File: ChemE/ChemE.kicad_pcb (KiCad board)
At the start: 2 copper layers, 36 x 26 mm, 11 parts, among them IC1 LF353P, J1 Circuit Battery, Q1 MTP3055E, U1 LM393N

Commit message: made prod
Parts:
- renumbered motor1 to motor, batt_car1 to motor_batt
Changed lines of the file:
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@@
 		(descr "Through hole straight pin header, 1x02, 2.54mm pitch, single row")
 		(tags "Through hole pin header THT 1x02 2.54mm single row")
-		(property "Reference" "motor1"
+		(property "Reference" "motor"
 			(at -2.4384 1.1176 90)
 			(layer "F.SilkS")
@@
 		(descr "Through hole straight pin header, 1x02, 2.54mm pitch, single row")
 		(tags "Through hole pin header THT 1x02 2.54mm single row")
-		(property "Reference" "batt_car1"
-			(at 2.54 1.4224 180)
-			(layer "F.SilkS")
-			(effects
+		(property "Reference" "motor_batt"
+			(at 2.54 0.7576 180)
+			(layer "F.SilkS")
+			(effects

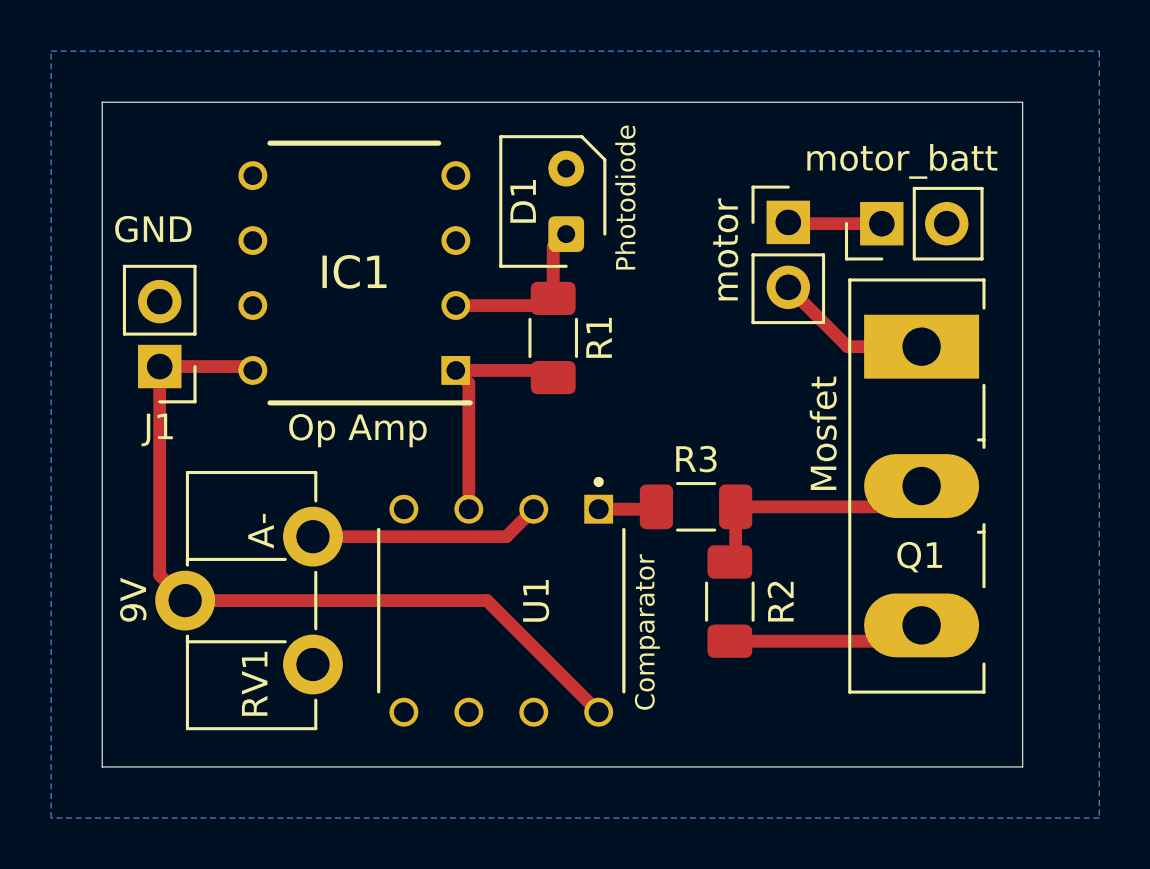
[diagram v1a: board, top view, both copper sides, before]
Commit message: increased trace width, made tht
increased trace width from .5mm to 1mm and made everything THT.
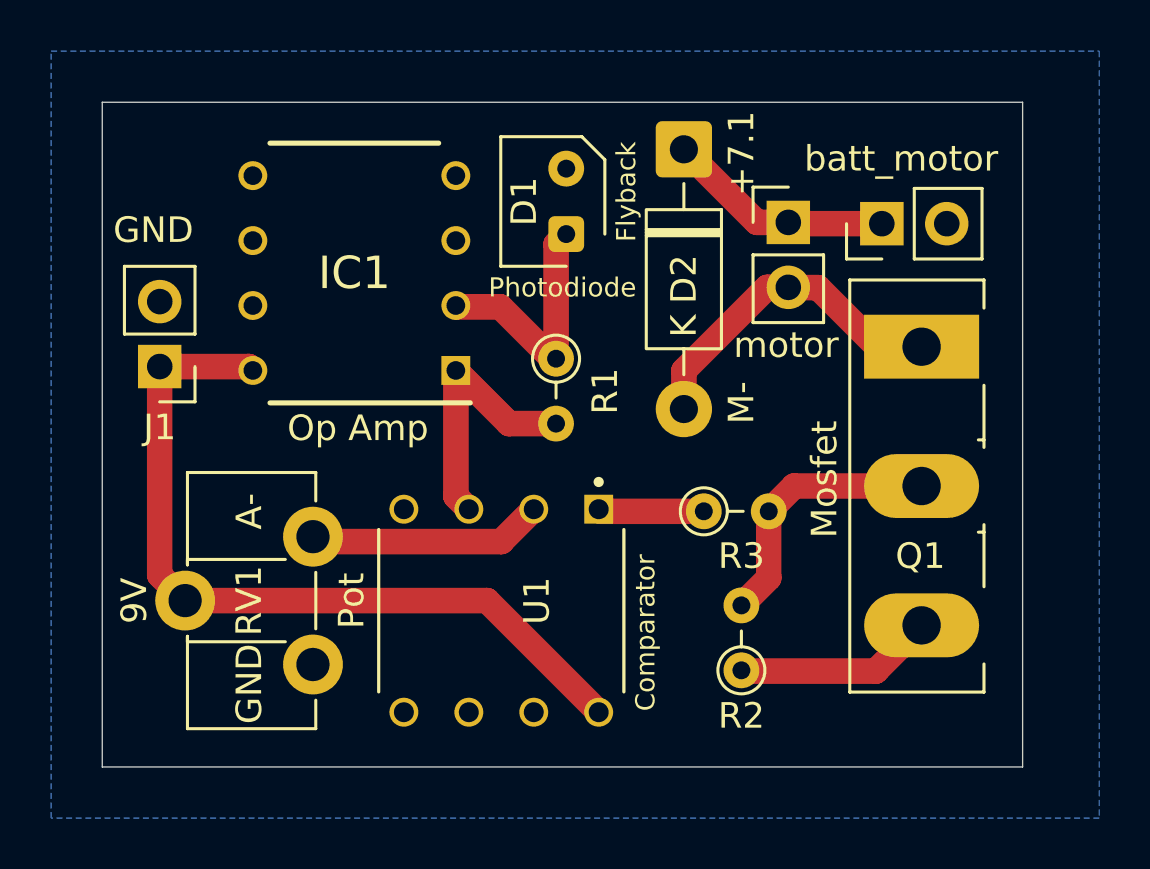
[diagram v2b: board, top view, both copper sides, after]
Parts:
- added D2: 1N4004, Diode_THT:D_DO-41_SOD81_P10.16mm_Horizontal, F.Cu at (172.8, 101.8)
- R1, R2, R3: footprint Resistor_SMD:R_1206_3216Metric_Pad1.30x1.75mm_HandSolder -> Resistor_THT:R_Axial_DIN0204_L3.6mm_D1.6mm_P2.54mm_Vertical
- moved R2 2.73 mm to (175.0, 122.2)
- moved R1 0.82 mm to (167.8, 110.0)
- moved R3 0.35 mm to (173.5, 116.0)
- renumbered motor_batt to batt_motor
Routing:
- net Net-(D2-A): track 6.18 -> 13.8 mm
- net +7.1V: track 3.68 -> 8.95 mm
- net Net-(D1-K): track 6.65 -> 9.82 mm
- net Net-(U1-OUT_A): track 2.30 -> 4.15 mm
- net Net-(IC1-1OUT): track 9.56 -> 10.4 mm
- net Net-(Q1-G): track 9.86 -> 10.7 mm
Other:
- board text added: "+7.1"
- board text added: "Flyback"
- board text added: "M-"
- board text added: "Pot"

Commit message: redid pot with correct wiring
https://www.piher.net/wp-content/uploads/PIHER_PT-15_PTC-15.pdf

also made prod. should be good to order.
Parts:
- Pot: renamed from RV1; footprint Potentiometer_THT:Potentiometer_ACP_CA9-H5_Horizontal -> Potentiometer_THT:Potentiometer_Piher_PT-6-H_Horizontal
- moved Pot 4.99 mm to (153.2, 122.0), turned to 90 degrees
- renumbered J1 to +9V, motor to motor1, batt_motor to motor_car1
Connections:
- Pot pad 1: GND -> +9V
- Pot pad 2: +9V -> Net-(U1-NEG_A)
- Pot pad 3: Net-(U1-NEG_A) -> GND
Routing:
- net Net-(U1-NEG_A): track 9.24 -> 12.6 mm
- net +9V: track 31.3 -> 33.4 mm
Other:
- board text removed: "Pot"
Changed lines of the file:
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@@
 	(net 14 "unconnected-(U1-OUT_B-Pad7)")
 	(net 15 "Net-(D2-A)")
-	(footprint "Potentiometer_THT:Potentiometer_ACP_CA9-H5_Horizontal"
-		(layer "F.Cu")
-		(at 158.242 121.9924 180)
-		(descr "Potentiometer, horizontal, ACP CA9-H5, http://www.acptechnologies.com/wp-content/uploads/2017/05/02-ACP-CA9-CE9.pdf")
-		(tags "Potentiometer horizontal ACP CA9-H5")
-		(property "Reference" "RV1"
-			(at 2.5 2.495 270)
+	(footprint "Potentiometer_THT:Potentiometer_Piher_PT-6-H_Horizontal"
+		(layer "F.Cu")
+		(at 153.25 121.95 90)
+		(descr "Potentiometer, horizontal, Piher PT-6-H, http://www.piher-nacesa.com/pdf/11-PT6v03.pdf")
+		(tags "Potentiometer horizontal Piher PT-6-H")
+		(property "Reference" "Pot"
+			(at 0.85 2.5 180)
 			(layer "F.SilkS")
 			(effects
@@
 		)
 		(property "Value" "10k pot"
-			(at 0 8.65 0)
-			(layer "F.Fab")
-			(hide yes)
+			(at 0 7.06 90)
+			(layer "F.Fab")
 			(effects
 				(font
@@
 		)
 		(property "Datasheet" "~"
-			(at 0 0 0)
+			(at 0 0 90)
 			(layer "F.Fab")
 			(hide yes)
@@
 		)
 		(property "Description" "Potentiometer"
-			(at 0 0 0)
+			(at 0 0 90)
 			(layer "F.Fab")
 			(hide yes)
@@
 		(attr through_hole)
 		(fp_line
-			(start 4.91 7.51)
-			(end -0.11 7.51)
-			(stroke
-				(width 0.12)
-				(type solid)
-			)
-			(layer "F.SilkS")
-		)
-		(fp_line
-			(start 4.91 4.11)
-			(end 1.081 4.11)
-			(stroke
-				(width 0.12)
-				(type solid)
-			)
-			(layer "F.SilkS")
-		)
-		(fp_line
-			(start 4.91 3.897)
-			(end 4.91 7.51)
-			(stroke
-				(width 0.12)
-				(type solid)
-			)
-			(layer "F.SilkS")
-		)
-		(fp_line
-			(start 4.91 3.897)
-			(end 4.91 4.11)
-			(stroke
-				(width 0.12)
-				(type solid)
-			)
-			(layer "F.SilkS")
-		)
-		(fp_line
-			(start 4.91 0.89)
-			(end 4.91 1.103)
-			(stroke
-				(width 0.12)
-				(type solid)
-			)
-			(layer "F.SilkS")
-		)
-		(fp_line
-			(start 4.91 -2.51)
-			(end 4.91 1.103)
-			(stroke
-				(width 0.12)
-				(type solid)
-			)
-			(layer "F.SilkS")
-		)
-		(fp_line
-			(start 1.081 0.89)
-			(end 4.91 0.89)
-			(stroke
-				(width 0.12)
-				(type solid)
-			)
-			(layer "F.SilkS")
-		)
-		(fp_line
-			(start -0.11 7.51)
-			(end -0.11 6.396)
-			(stroke
-				(width 0.12)
-				(type solid)
-			)
-			(layer "F.SilkS")
-		)
-		(fp_line
-			(start -0.11 3.604)
-			(end -0.11 1.396)
-			(stroke
-				(width 0.12)
-				(type solid)
-			)
-			(layer "F.SilkS")
-		)
-		(fp_line
-			(start -0.11 3.604)
-			(end -0.11 1.396)
-			(stroke
-				(width 0.12)
-				(type solid)
-			)
-			(layer "F.SilkS")
-		)
-		(fp_line
-			(start -0.11 -1.396)
-			(end -0.11 -2.51)
-			(stroke
-				(width 0.12)
-				(type solid)
-			)
-			(layer "F.SilkS")
-		)
-		(fp_line
-			(start -0.11 -2.51)
-			(end 4.91 -2.51)
+			(start 3.61 -0.76)
+			(end 3.61 5.76)
+			(stroke
+				(width 0.12)
+				(type solid)
+			)
+			(layer "F.SilkS")
+		)
+		(fp_line
+			(start 0.71 -0.76)
+			(end 3.61 -0.76)
+			(stroke
+				(width 0.12)
+				(type solid)
+			)
+			(layer "F.SilkS")
+		)
+		(fp_line
+			(start 3.61 1.39)
+			(end 3.61 3.61)
+			(stroke
+				(width 0.12)
+				(type solid)
+			)
+			(layer "F.SilkS")
+		)
+		(fp_line
+			(start -0.11 1.39)
+			(end 3.61 1.39)
+			(stroke
+				(width 0.12)
+				(type solid)
+			)
+			(layer "F.SilkS")
+		)
+		(fp_line
+			(start 3.61 3.61)
+			(end -0.11 3.61)
+			(stroke
+				(width 0.12)
+				(type solid)
+			)
+			(layer "F.SilkS")
+		)
+		(fp_line
+			(start -0.11 3.61)
+			(end -0.11 1.39)
+			(stroke
+				(width 0.12)
+				(type solid)
+			)
+			(layer "F.SilkS")
+		)
+		(fp_line
+			(start -0.11 3.966)
+			(end -0.11 1.034)
+			(stroke
+				(width 0.12)
+				(type solid)
+			)
+			(layer "F.SilkS")
+		)
+		(fp_line
+			(start 3.61 5.76)
+			(end 0.71 5.76)
 			(stroke
 				(width 0.12)
@@
 		)
 		(fp_rect
-			(start -1.42 -2.66)
-			(end 6.42 7.65)
+			(start -1.06 -1.06)
+			(end 3.76 6.06)
 			(stroke
 				(width 0.05)
@@
 		)
 		(fp_rect
-			(start 0 1)
-			(end 4.8 4)
+			(start 0 -0.65)
+			(end 3.5 5.65)
 			(stroke
 				(width 0.1)
@@
 		)
 		(fp_rect
-			(start 0 -2.4)
-			(end 4.8 7.4)
+			(start 0 1.5)
+			(end 3.5 3.5)
 			(stroke
 				(width 0.1)
@@
 			(layer "F.Fab")
 		)
+		(fp_text user "${REFERENCE}"
+			(at 1.75 2.5 90)
+			(layer "F.Fab")
+			(effects
+				(font
+					(size 0.78 0.78)
+					(thickness 0.12)
+				)
+			)
+		)
 		(pad "1" thru_hole circle
-			(at 0 0 180)
-			(size 2.34 2.34)
-			(drill 1.3)
-			(layers "*.Cu" "*.Mask")
-			(remove_unused_layers no)
-			(net 1 "GND")
+			(at 0 0 90)
+			(size 1.62 1.62)
+			(drill 0.9)
+			(layers "*.Cu" "*.Mask")
+			(remove_unused_layers no)
+			(net 3 "+9V")
 			(pinfunction "1")
 			(pintype "passive")
 		)
 		(pad "2" thru_hole circle
-			(at 5 2.5 180)
-			(size 2.34 2.34)
-			(drill 1.3)
-			(layers "*.Cu" "*.Mask")
-			(remove_unused_layers no)
-			(net 3 "+9V")
+			(at 2.5 2.5 90)
+			(size 1.62 1.62)
+			(drill 0.9)
+			(layers "*.Cu" "*.Mask")
+			(remove_unused_layers no)
+			(net 8 "Net-(U1-NEG_A)")
 			(pinfunction "2")
 			(pintype "passive")
 		)
 		(pad "3" thru_hole circle
-			(at 0 5 180)
-			(size 2.34 2.34)
-			(drill 1.3)
-			(layers "*.Cu" "*.Mask")
-			(remove_unused_layers no)
-			(net 8 "Net-(U1-NEG_A)")
+			(at 0 5 90)
+			(size 1.62 1.62)
+			(drill 0.9)
+			(layers "*.Cu" "*.Mask")
+			(remove_unused_layers no)
+			(net 1 "GND")
 			(pinfunction "3")
 			(pintype "passive")
 		)
 		(embedded_fonts no)
-		(model "${KICAD9_3DMODEL_DIR}/Potentiometer_THT.3dshapes/Potentiometer_ACP_CA9-H5_Horizontal.step"
+		(model "${KICAD9_3DMODEL_DIR}/Potentiometer_THT.3dshapes/Potentiometer_Piher_PT-6-H_Horizontal.step"
 			(offset
 				(xyz 0 0 0)
@@
 		(descr "Through hole straight pin header, 1x02, 2.54mm pitch, single row")
 		(tags "Through hole pin header THT 1x02 2.54mm single row")
-		(property "Reference" "J1"
-			(at 0 -2.38 0)
+		(property "Reference" "+9V"
+			(at 0.1476 -2.6124 0)
 			(layer "F.SilkS")
 			(effects
@@
 			(layer "F.Fab")
 		)
-		(fp_text user "${REFERENCE}"
-			(at 1.27 -1.92 0)
-			(layer "F.Fab")
-			(effects
-				(font
-					(size 1 1)
-					(thickness 0.15)
-				)
-			)
-		)
 		(pad "1" thru_hole circle
 			(at 0 0)
@@
 		(descr "Through hole straight pin header, 1x02, 2.54mm pitch, single row")
 		(tags "Through hole pin header THT 1x02 2.54mm single row")
-		(property "Reference" "motor"
+		(property "Reference" "motor1"
 			(at -0.0848 4.8012 180)
 			(layer "F.SilkS")
@@
 		(descr "Through hole straight pin header, 1x02, 2.54mm pitch, single row")
 		(tags "Through hole pin header THT 1x02 2.54mm single row")
-		(property "Reference" "batt_motor"
+		(property "Reference" "motor_car1"
 			(at 2.54 0.7576 180)
 			(layer "F.SilkS")
@@
 		(fill no)
 		(layer "Edge.Cuts")
-	)
-	(gr_text "Pot"
-		(at 159.75 119.5 90)
-		(layer "F.SilkS")
-		(effects
-			(font
-				(size 1 1)
-				(thickness 0.15)
-			)
-		)
 	)
 	(gr_text "Photodiode"
@@
 	)
 	(gr_text "9V"
-		(at 151.25 119.5 90)
+		(at 153.25 123.75 0)
 		(layer "F.SilkS")
 		(effects
@@
 	)
 	(gr_text "A-"
-		(at 155.75 116 90)
+		(at 155.85 117.5 0)
 		(layer "F.SilkS")
 		(effects
@@
 	)
 	(gr_text "GND"
-		(at 155.75 122.75 90)
+		(at 158.3 123.6 0)
 		(layer "F.SilkS")
 		(effects
@@
 	(segment
 		(start 152.2476 110.3376)
+		(end 152.2476 120.9476)
+		(width 1)
+		(layer "F.Cu")
+		(net 3)
+	)
+	(segment
+		(start 161.273605 122.592)
+		(end 168.152 122.592)
+		(width 1)
+		(layer "F.Cu")
+		(net 3)
+	)
+	(segment
+		(start 152.2476 110.3376)
 		(end 155.7376 110.3376)
 		(width 1)
@@
 	)
 	(segment
-		(start 152.2476 110.3376)
-		(end 152.2476 118.498)
+		(start 160.404605 123.461)
+		(end 161.273605 122.592)
 		(width 1)
 		(layer "F.Cu")
@@
 	)
 	(segment
-		(start 165.0524 119.4924)
+		(start 152.2476 120.9476)
+		(end 153.25 121.95)
+		(width 1)
+		(layer "F.Cu")
+		(net 3)
+	)
+	(segment
+		(start 154.761 123.461)
+		(end 160.404605 123.461)
+		(width 1)
+		(layer "F.Cu")
+		(net 3)
+	)
+	(segment
+		(start 168.152 122.592)
 		(end 169.418 123.858)
 		(width 1)
@@
 	)
 	(segment
-		(start 152.2476 118.498)
-		(end 153.242 119.4924)
-		(width 1)
-		(layer "F.Cu")
-		(net 3)
-	)
-	(segment
-		(start 153.242 119.4924)
-		(end 165.0524 119.4924)
+		(start 153.25 121.95)
+		(end 154.761 123.461)
 		(width 1)
 		(layer "F.Cu")
@@
 	)
 	(segment
-		(start 166.878 115.918)
-		(end 165.612 117.184)
+		(start 163.346 119.45)
+		(end 166.878 115.918)
 		(width 1)
 		(layer "F.Cu")
@@
 	)
 	(segment
-		(start 158.4336 117.184)
-		(end 158.242 116.9924)
-		(width 1)
-		(layer "F.Cu")
-		(net 8)
-	)
-	(segment
-		(start 165.612 117.184)
-		(end 158.4336 117.184)
-		(width 1)
-		(layer "F.Cu")
+		(start 155.75 119.45)
+		(end 163.346 119.45)
+		(width 1)
+		(layer "F.Cu")
